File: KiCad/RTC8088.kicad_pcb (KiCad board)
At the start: 2 copper layers, 86.4 x 38.1 mm, 9 parts, among them SW1 Address Select, U1 DS12885, U2 ATF16V8B, Y1 32768Hz

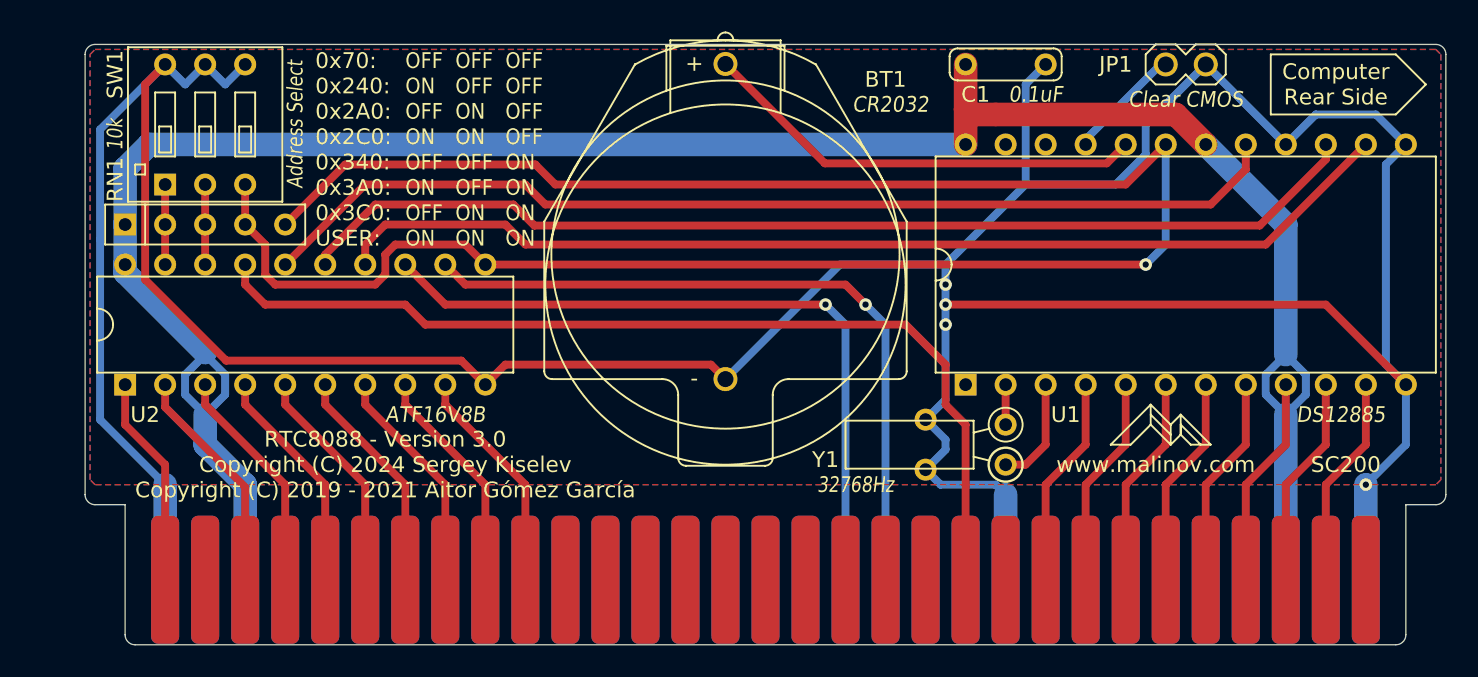
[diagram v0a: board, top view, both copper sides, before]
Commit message: Fix an error in the layout. Update GitHub repo. Remove unised pads on card edge connector
Signed-off-by: Sergey Kiselev <sergey.kiselev@intel.com>
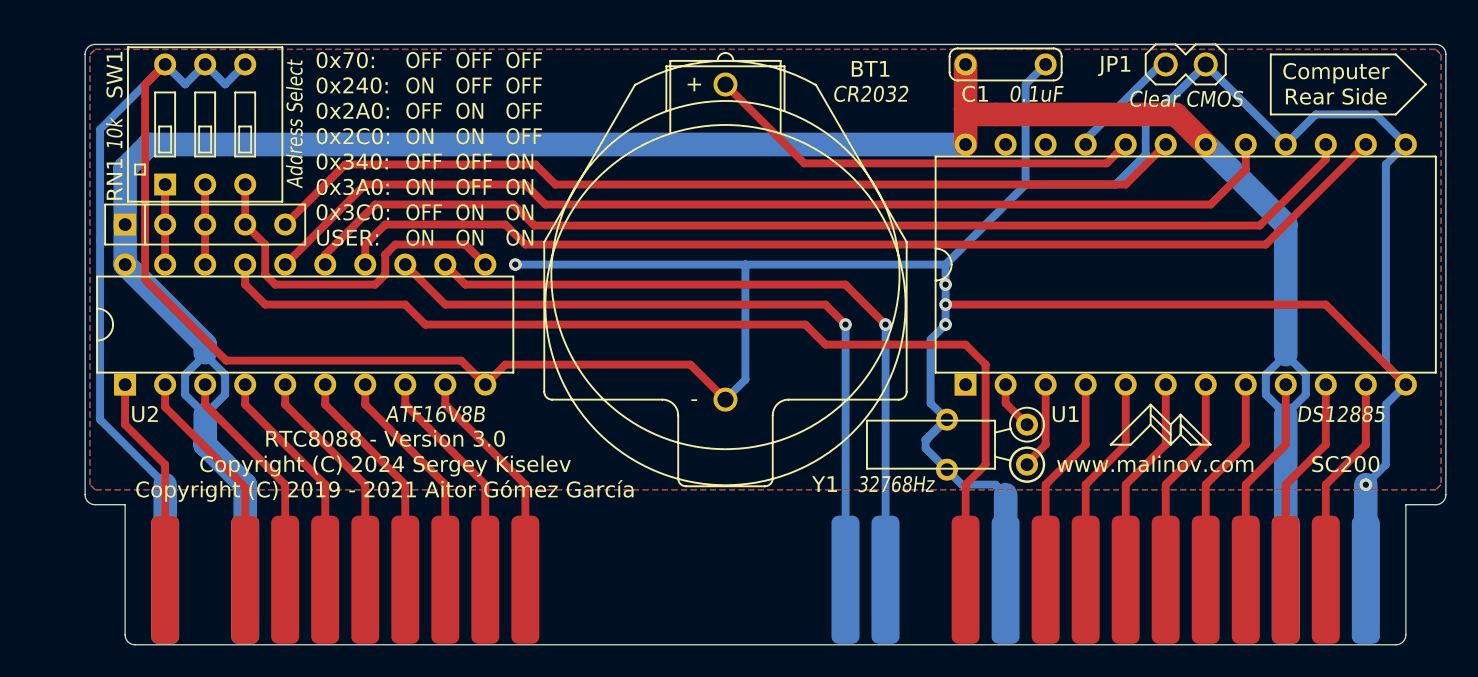
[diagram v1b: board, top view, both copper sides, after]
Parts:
- moved Y1 1.36 mm to (169.0, 82.5)
- moved BT1 1.30 mm to (149.9, 73.7)
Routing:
- net /AS2: track 72.9 -> 22.8 mm, vias 1 -> 0
- net GND: track 249.2 -> 270.0 mm, vias 4 -> 5
- net /AEN: track 61.7 -> 64.2 mm
- net Net-(U1-Pad3): track 6.88 -> 5.61 mm
- net Net-(U1-Pad2): track 2.54 -> 3.10 mm
- net Net-(BT1-Pad1): track 28.5 -> 28.0 mm
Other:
- board text added: "Copyright (C) 2024 Sergey Kiselev Copyright (C) 2019 - 2021 Aitor Gómez García Design files and documentation: https://github.com/spark2k06/RTC8088 Licensed under CERN-OHL-S: https://cern-ohl.web.cern.ch"
- board text removed: "Copyright (C) 2024 Sergey Kiselev Copyright (C) 2019 - 2021 Aitor Gómez García Design files and documentation: https://github.com/skiselev/RTC8088 Licensed under CERN-OHL-S: https://cern-ohl.web.cern.ch"

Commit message: Update silkscreen
Signed-off-by: Sergey Kiselev <sergey.kiselev@intel.com>
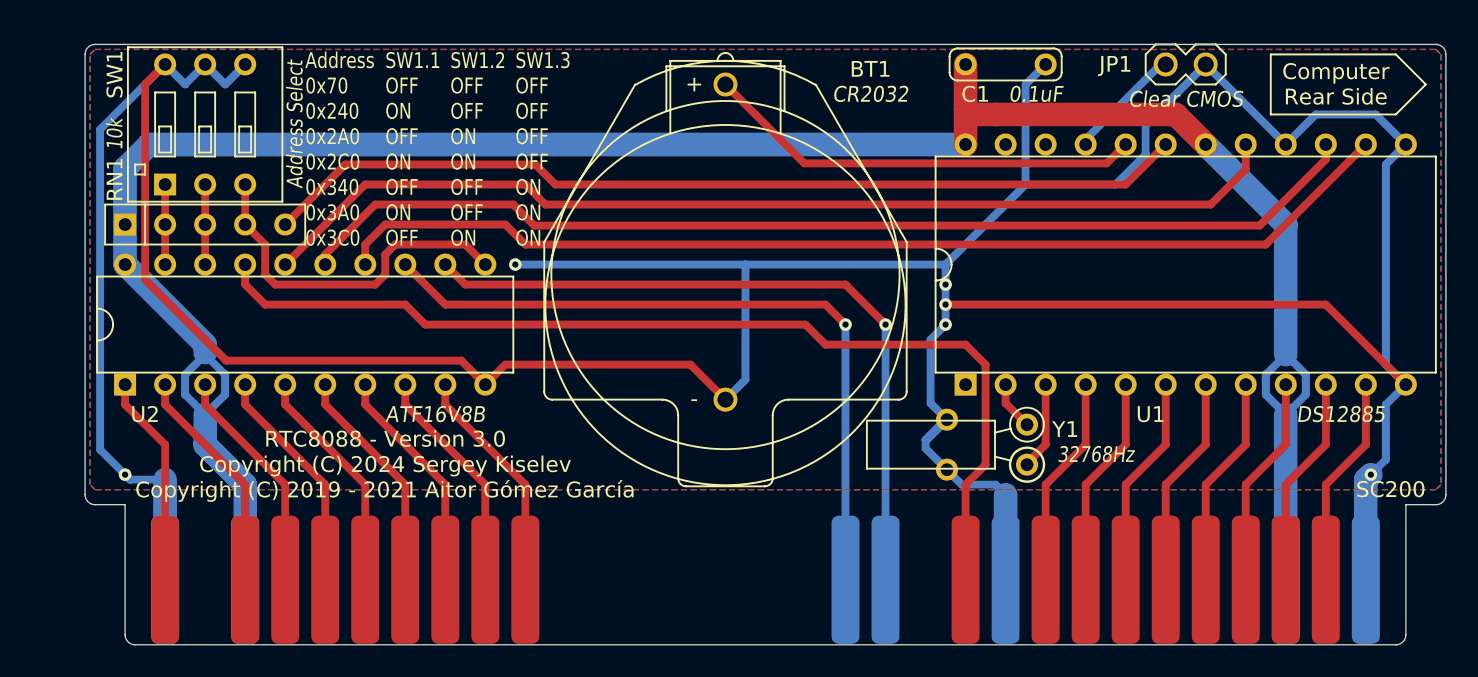
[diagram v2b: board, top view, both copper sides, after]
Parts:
- added REF**: KiCad-Logo2_5mm_SilkScreen, Symbol:KiCad-Logo2_5mm_SilkScreen, B.Cu at (118.4, 82.5)
- added REF**: OSHW-Logo2_7.3x6mm_SilkScreen, Symbol:OSHW-Logo2_7.3x6mm_SilkScreen, B.Cu at (130.8, 82.9)
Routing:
- net GND: track 270.0 -> 271.3 mm, vias 5 -> 6
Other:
- board text added: "Address 0x70 0x240 0x2A0 0x2C0 0x340 0x3A0 0x3C0"
- board text added: "SW1.1 OFF ON OFF ON OFF ON OFF"
- board text added: "SW1.2 OFF OFF ON ON OFF OFF ON"
- board text added: "SW1.3 OFF OFF OFF OFF ON ON ON"
- board text removed: "0x70: 0x240: 0x2A0: 0x2C0: 0x340: 0x3A0: 0x3C0: USER:"
- board text removed: "OFF OFF OFF OFF ON ON ON ON"
- board text removed: "OFF OFF ON ON OFF OFF ON ON"
- board text removed: "OFF ON OFF ON OFF ON OFF ON"
